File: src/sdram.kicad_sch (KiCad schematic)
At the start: 7 parts, among them U11 IS42S16160J-*BL

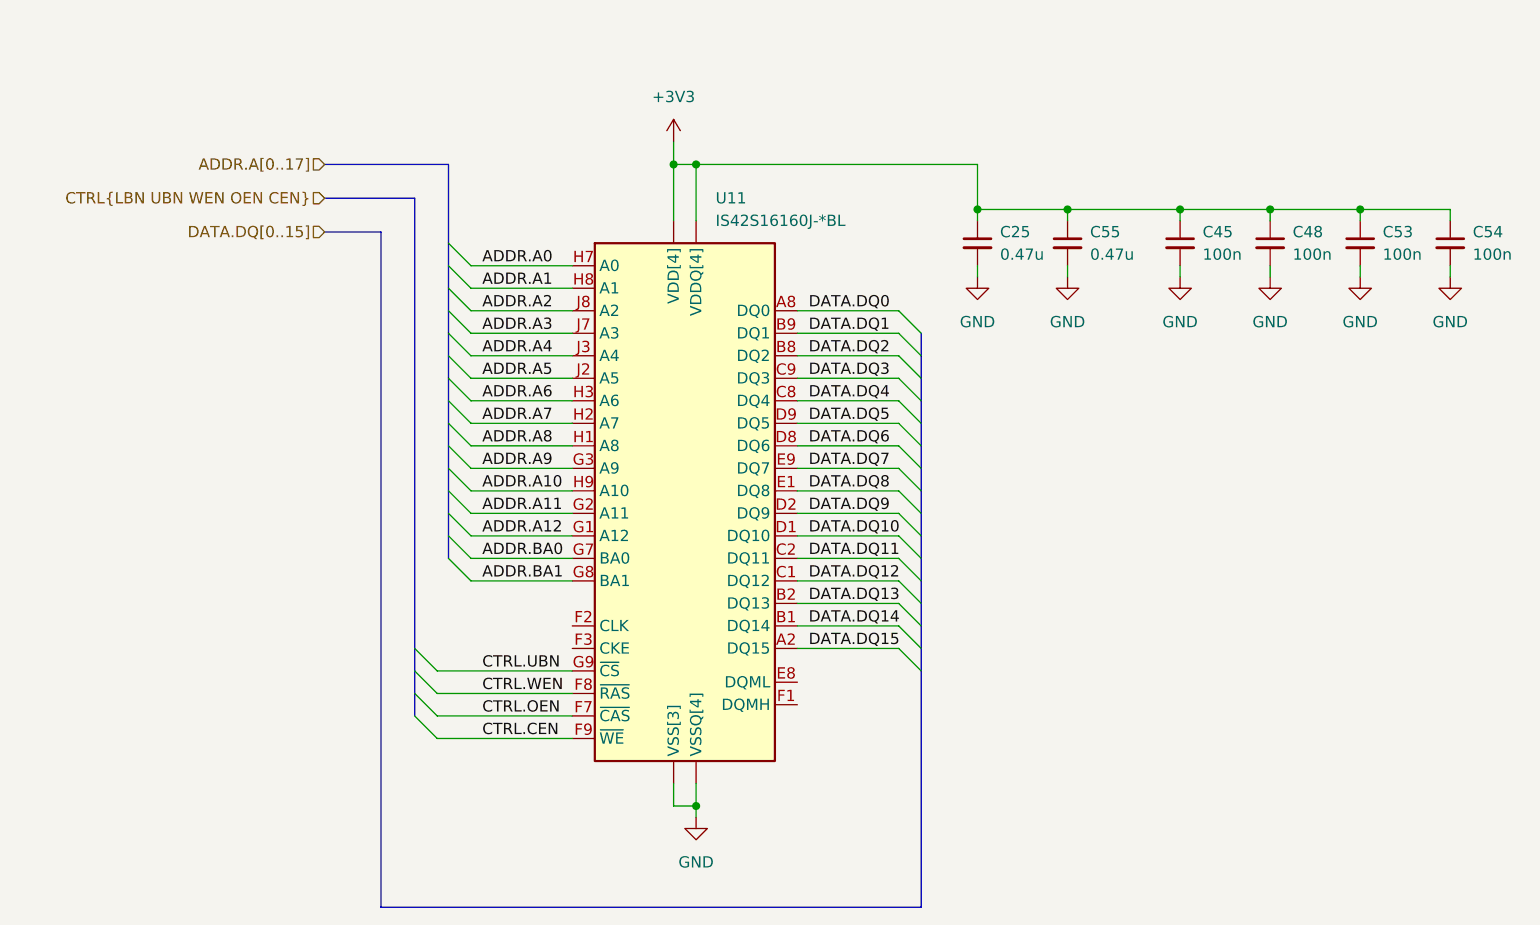
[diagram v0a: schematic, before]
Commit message: Adds DDR2 schematic
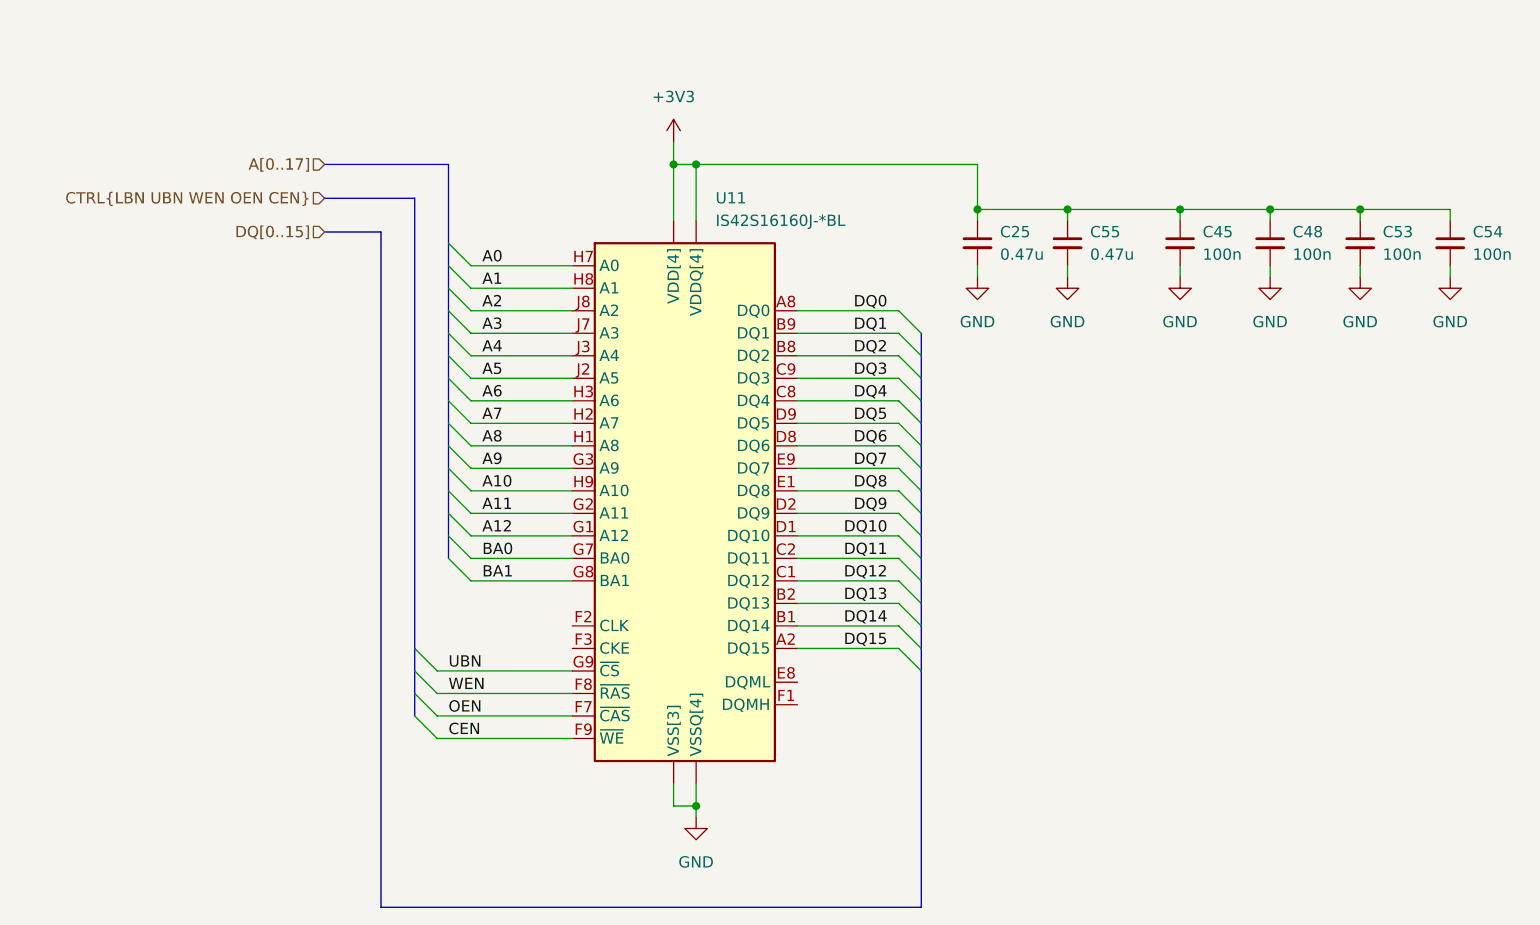
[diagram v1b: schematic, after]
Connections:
- net ADDR.A0 renamed A0
- net ADDR.A1 renamed A1
- net ADDR.A10 renamed A10
- net ADDR.A11 renamed A11
- net ADDR.A12 renamed A12
- net ADDR.A2 renamed A2
- net ADDR.A3 renamed A3
- net ADDR.A4 renamed A4
- net ADDR.A5 renamed A5
- net ADDR.A6 renamed A6
- net ADDR.A7 renamed A7
- net ADDR.A8 renamed A8
- net ADDR.A9 renamed A9
- net ADDR.BA0 renamed BA0
- net ADDR.BA1 renamed BA1
- net CTRL.CEN renamed CEN
- net CTRL.OEN renamed OEN
- net CTRL.UBN renamed UBN
- net CTRL.WEN renamed WEN
- net DATA.DQ0 renamed DQ0
- net DATA.DQ1 renamed DQ1
- net DATA.DQ10 renamed DQ10
- net DATA.DQ11 renamed DQ11
- net DATA.DQ12 renamed DQ12
- net DATA.DQ13 renamed DQ13
- net DATA.DQ14 renamed DQ14
- net DATA.DQ15 renamed DQ15
- net DATA.DQ2 renamed DQ2
- net DATA.DQ3 renamed DQ3
- net DATA.DQ4 renamed DQ4
- net DATA.DQ5 renamed DQ5
- net DATA.DQ6 renamed DQ6
- net DATA.DQ7 renamed DQ7
- net DATA.DQ8 renamed DQ8
- net DATA.DQ9 renamed DQ9

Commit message: Finishes the ram schematic
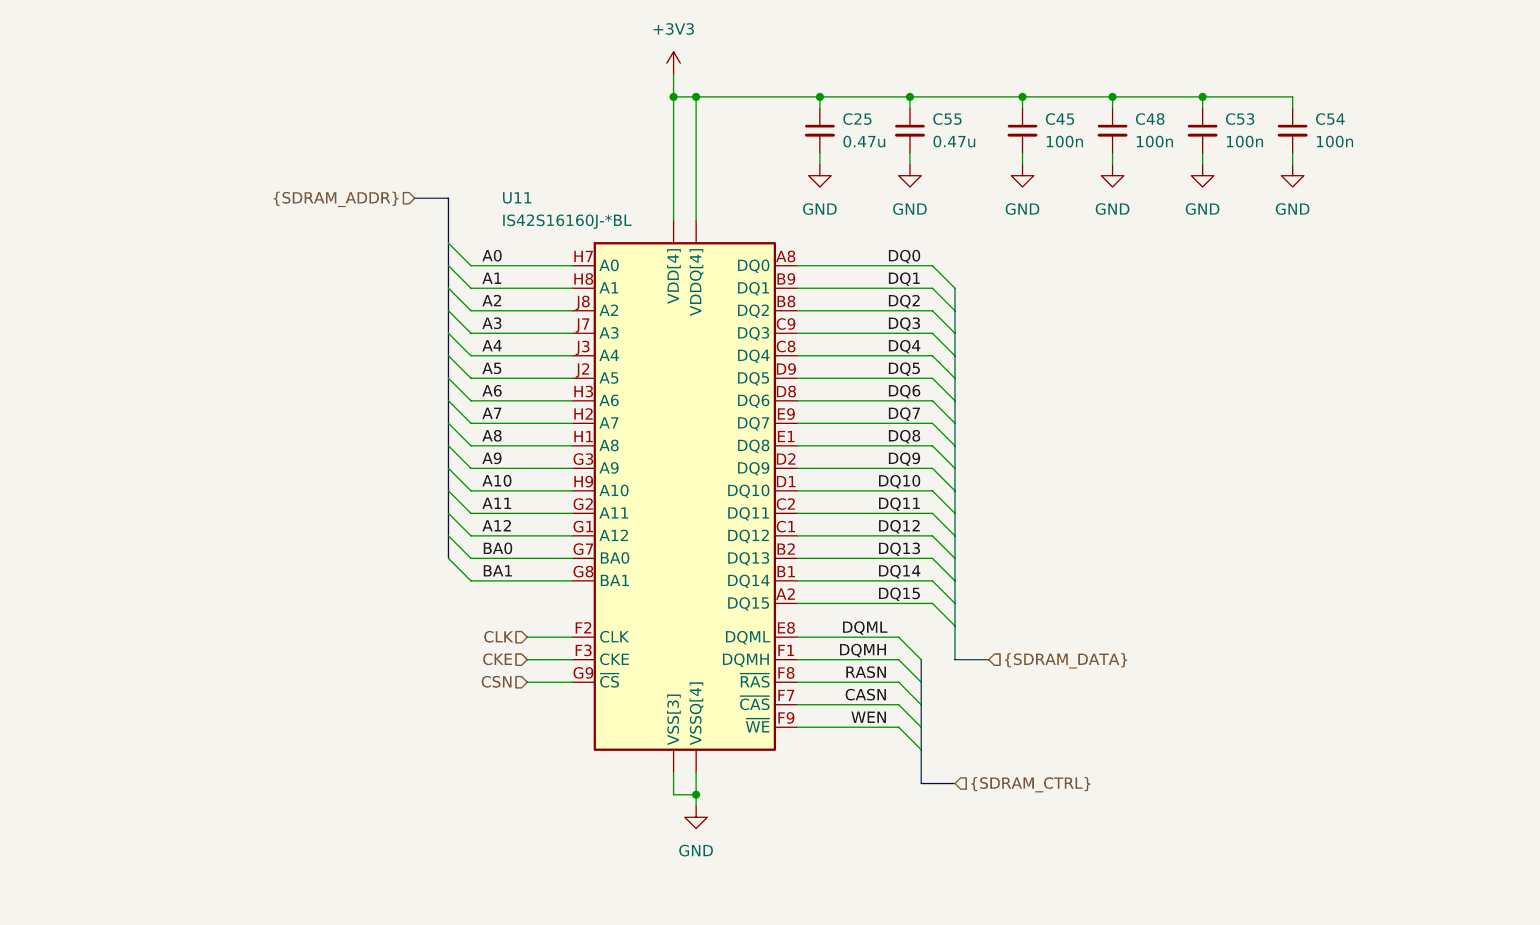
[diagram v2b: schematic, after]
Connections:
- net CEN is gone; now on net WEN: U11.F9 (~{WE})
- net WEN: no longer U11.F8 (~{RAS})
- net DQML: now reaches U11.E8 (DQML)
- net DQMH: now reaches U11.F1 (DQMH)
- net CLK: now reaches U11.F2 (CLK)
- net CKE: now reaches U11.F3 (CKE)
- net OEN renamed CASN
- net UBN renamed CSN
- new net RASN: U11.F8 (~{RAS})
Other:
- moved on the sheet: C25, C45, C48, C53, C54, C55, U11
